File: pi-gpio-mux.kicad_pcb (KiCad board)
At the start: 2 copper layers, 65 x 56 mm, 35 parts, among them J1 Raspberry_Pi_2_3, J2 Raw, J3 Buffered, J4 Register-1, J5 Register-2, J6 Clk1, J7 Clk2, U1 74AHCT245, U10 74AHCT574, U11 74AHCT574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

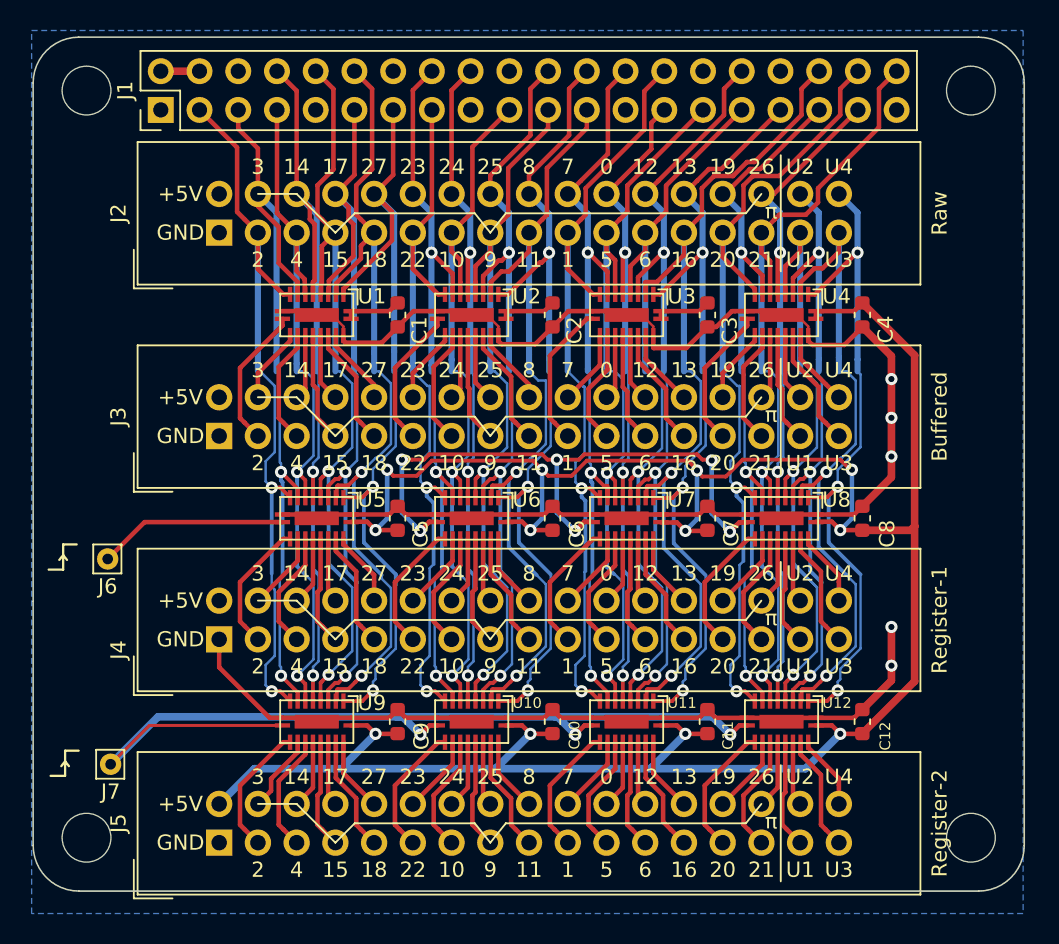
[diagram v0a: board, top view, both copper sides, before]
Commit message: Solve routing of VCC for buffers.
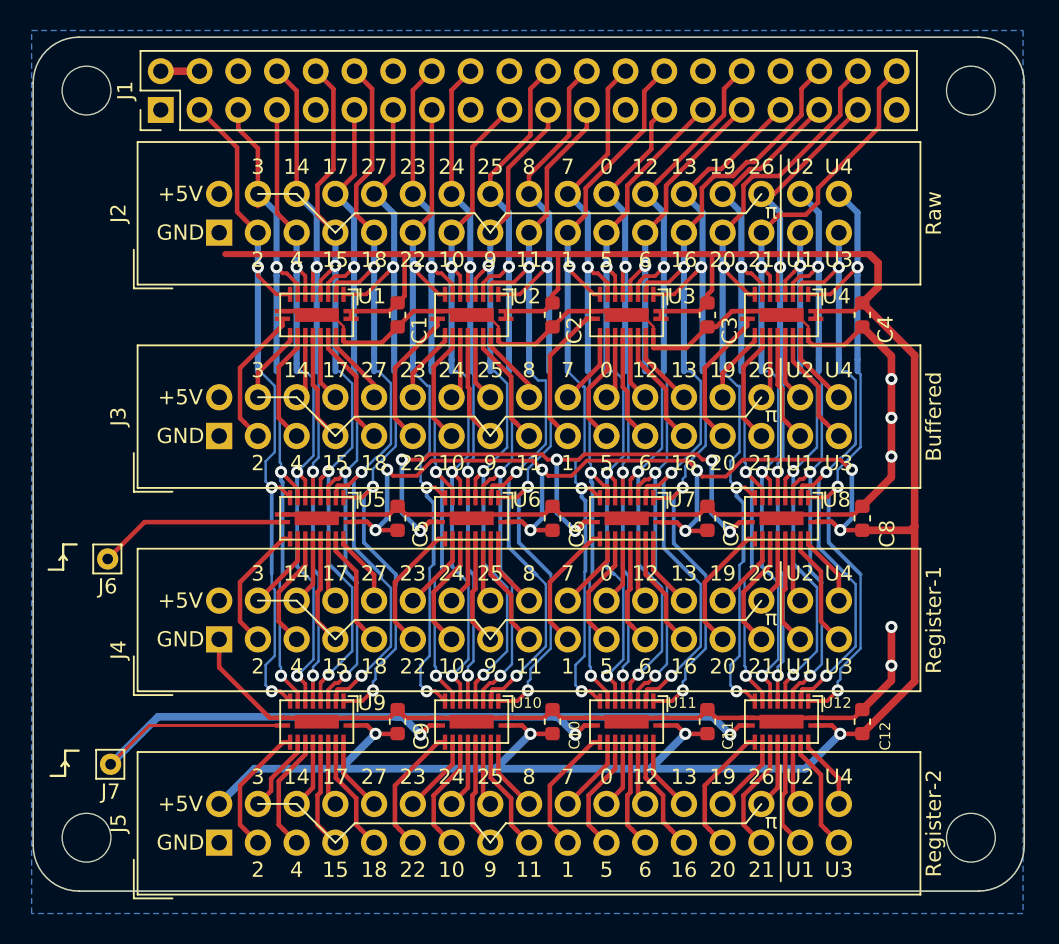
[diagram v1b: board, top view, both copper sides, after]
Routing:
- net VCC: track 180.9 -> 237.2 mm
- net Pin8-GPIO14: track 51.7 -> 46.4 mm, vias 2 -> 3
- net Pin11-GPIO17: track 51.5 -> 46.6 mm, vias 2 -> 3
- net Pin13-GPIO27: track 54.4 -> 50.0 mm, vias 2 -> 3
- net Pin5-GPIO3: track 50.3 -> 45.9 mm, vias 2 -> 3
- net Pin15-GPIO22: track 48.4 -> 46.1 mm, vias 2 -> 3
- net Pin28-GPIO1: track 52.9 -> 50.6 mm, vias 2 -> 3
- net Pin7-GPIO4: track 48.2 -> 45.9 mm, vias 2 -> 3
- net Pin19-GPIO10: track 49.0 -> 46.7 mm, vias 2 -> 3
- net Pin40-GPIO21: track 54.7 -> 52.4 mm, vias 2 -> 3
- net Pin29-GPIO5: track 50.1 -> 47.8 mm, vias 2 -> 3
- net Pin21-GPIO9: track 50.6 -> 48.4 mm, vias 2 -> 3
- net Pin10-GPIO15: track 51.9 -> 49.7 mm, vias 2 -> 3
- net Pin31-GPIO6: track 51.9 -> 49.7 mm, vias 2 -> 3
- net User1: track 41.1 -> 39.0 mm, vias 2 -> 3
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
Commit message: Route VCC and GND. No unrouted left.
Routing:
- net VCC: track 237.2 -> 350.9 mm, vias 12 -> 13
- net /CLK1: track 53.0 -> 70.9 mm
- net /CLK2: track 62.7 -> 53.3 mm, vias 3 -> 4
- net GND: track 155.2 -> 162.6 mm, vias 5 -> 7
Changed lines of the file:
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@@
     (thickness 1.6)
     (drawings 21)
-    (tracks 1649)
+    (tracks 1692)
     (zones 0)
     (modules 35)
@@
   )
   (setup
-    (last_trace_width 0.3)
+    (last_trace_width 0.25)
     (user_trace_width 0.16)
     (user_trace_width 0.2)
@@
   (via (at 256.2864 135.2172) (size 0.8) (drill 0.4) (layers F.Cu B.Cu) (net 1))
   (via (at 256.2864 132.6772) (size 0.8) (drill 0.4) (layers F.Cu B.Cu) (net 1))
+  (via (at 213.3984 124.5492) (size 0.8) (drill 0.4) (layers F.Cu B.Cu) (net 1))
+  (segment (start 216.35 125.3025) (end 214.1517 125.3025) (width 0.25) (layer F.Cu) (net 1))
+  (segment (start 214.1517 125.3025) (end 213.3984 124.5492) (width 0.25) (layer F.Cu) (net 1))
+  (via (at 212.23 111.9508) (size 0.8) (drill 0.4) (layers F.Cu B.Cu) (net 1))
+  (segment (start 216.35 111.9675) (end 212.2467 111.9675) (width 0.25) (layer F.Cu) (net 1))
+  (segment (start 212.2467 111.9675) (end 212.23 111.9508) (width 0.25) (layer F.Cu) (net 1))
   (segment (start 243.884799 122.815599) (end 243.4848 122.4156) (width 0.25) (layer F.Cu) (net 2))
   (segment (start 245.423799 122.815599) (end 243.884799 122.815599) (width 0.25) (layer F.Cu) (net 2))
@@
   (segment (start 214.5114 141.9736) (end 220.4724 141.9736) (width 0.5) (layer B.Cu) (net 2))
   (segment (start 220.4724 141.9736) (end 230.1244 141.9736) (width 0.5) (layer B.Cu) (net 2))
-  (segment (start 210.91 96.23) (end 208.37 96.23) (width 0.5) (layer F.Cu) (net 2))
+  (segment (start 210.91 96.23) (end 208.37 96.23) (width 1) (layer F.Cu) (net 2))
   (segment (start 254.38 111.43) (end 257.8104 114.8604) (width 0.5) (layer F.Cu) (net 2))
   (segment (start 257.8104 136.2446) (end 254.38 139.675) (width 0.5) (layer F.Cu) (net 2))
@@
   (segment (start 255.41 108.8012) (end 254.902 108.2932) (width 0.5) (layer F.Cu) (net 2))
   (segment (start 254.902 108.2932) (end 254.836276 108.227476) (width 0.4) (layer F.Cu) (net 2))
-  (segment (start 224.254674 108.227474) (end 212.600526 108.227474) (width 0.4) (layer F.Cu) (net 2))
   (segment (start 254.836272 108.227472) (end 254.902 108.2932) (width 0.4) (layer F.Cu) (net 2))
   (segment (start 234.4296 110.5229) (end 234.4296 108.344) (width 0.3) (layer F.Cu) (net 2))
@@
   (segment (start 224.361612 108.309896) (end 224.361612 110.968388) (width 0.3) (layer F.Cu) (net 2))
   (segment (start 224.3204 108.268684) (end 224.361612 108.309896) (width 0.3) (layer F.Cu) (net 2))
+  (segment (start 223.2156 122.3648) (end 222.606 121.7552) (width 0.2) (layer F.Cu) (net 2))
+  (segment (start 222.606 121.7552) (end 214.8208 121.7552) (width 0.2) (layer F.Cu) (net 2))
+  (segment (start 207.520001 97.079999) (end 207.171999 97.079999) (width 1) (layer F.Cu) (net 2))
+  (segment (start 207.171999 97.079999) (end 206.5912 97.660798) (width 1) (layer F.Cu) (net 2))
+  (segment (start 201.1556 133.2406) (end 212.2 144.285) (width 1) (layer F.Cu) (net 2))
+  (segment (start 206.5912 97.660798) (end 206.5912 99.6572) (width 1) (layer F.Cu) (net 2))
+  (segment (start 208.37 96.23) (end 207.520001 97.079999) (width 1) (layer F.Cu) (net 2))
+  (segment (start 201.6128 130.95) (end 201.1556 130.4928) (width 1) (layer F.Cu) (net 2))
+  (segment (start 212.2 130.95) (end 201.6128 130.95) (width 1) (layer F.Cu) (net 2))
+  (segment (start 201.1556 105.0928) (end 201.1556 130.4928) (width 1) (layer F.Cu) (net 2))
+  (segment (start 201.1556 130.4928) (end 201.1556 133.2406) (width 1) (layer F.Cu) (net 2))
+  (segment (start 212.2 117.615) (end 210.0964 115.5114) (width 1) (layer F.Cu) (net 2))
+  (segment (start 210.978686 104.28) (end 212.2 104.28) (width 1) (layer F.Cu) (net 2))
+  (segment (start 210.0964 105.162286) (end 210.978686 104.28) (width 1) (layer F.Cu) (net 2))
+  (segment (start 210.1472 104.28) (end 206.0578 100.1906) (width 1) (layer F.Cu) (net 2))
+  (segment (start 212.2 104.28) (end 210.1472 104.28) (width 1) (layer F.Cu) (net 2))
+  (segment (start 206.5912 99.6572) (end 206.0578 100.1906) (width 1) (layer F.Cu) (net 2))
+  (segment (start 206.0578 100.1906) (end 201.1556 105.0928) (width 1) (layer F.Cu) (net 2))
+  (segment (start 210.538674 108.227474) (end 210.0964 107.7852) (width 0.4) (layer F.Cu) (net 2))
+  (segment (start 224.254674 108.227474) (end 210.538674 108.227474) (width 0.4) (layer F.Cu) (net 2))
+  (segment (start 210.0964 115.5114) (end 210.0964 107.7852) (width 1) (layer F.Cu) (net 2))
+  (segment (start 210.0964 107.7852) (end 210.0964 105.162286) (width 1) (layer F.Cu) (net 2))
+  (segment (start 214.8208 121.7552) (end 214.516 121.7552) (width 0.3) (layer F.Cu) (net 2))
+  (segment (start 214.516 121.7552) (end 213.8556 121.7552) (width 0.3) (layer F.Cu) (net 2))
+  (via (at 211.214 124.6) (size 0.8) (drill 0.4) (layers F.Cu B.Cu) (net 2))
+  (segment (start 213.8556 121.7552) (end 211.214 124.3968) (width 0.3) (layer F.Cu) (net 2))
+  (segment (start 211.214 124.3968) (end 211.214 124.6) (width 0.3) (layer F.Cu) (net 2))
+  (segment (start 211.214 129.964) (end 212.2 130.95) (width 0.3) (layer B.Cu) (net 2))
+  (segment (start 211.214 124.6) (end 211.214 129.964) (width 0.3) (layer B.Cu) (net 2))
   (segment (start 247.79264 128.70464) (end 247.79264 122.93376) (width 0.25) (layer B.Cu) (net 3))
   (segment (start 248.26 129.172) (end 247.79264 128.70464) (width 0.25) (layer B.Cu) (net 3))
@@
   (segment (start 234.3408 125.185147) (end 235.135391 125.979738) (width 0.3) (layer B.Cu) (net 132))
   (segment (start 236.67 125.7771) (end 236.138027 125.7771) (width 0.3) (layer F.Cu) (net 132))
-  (segment (start 207.3065 125.8025) (end 204.8895 128.2195) (width 0.3) (layer F.Cu) (net 132))
-  (segment (start 216.35 125.8025) (end 207.3065 125.8025) (width 0.3) (layer F.Cu) (net 132))
+  (segment (start 224.1808 121.7044) (end 223.755001 121.278601) (width 0.2) (layer F.Cu) (net 132))
+  (segment (start 207.3065 125.8025) (end 207.1945 125.9145) (width 0.3) (layer F.Cu) (net 132))
+  (segment (start 207.1945 125.9145) (end 204.8895 128.2195) (width 0.3) (layer F.Cu) (net 132))
+  (segment (start 216.35 125.8025) (end 212.4673 125.8025) (width 0.3) (layer F.Cu) (net 132))
+  (segment (start 223.755001 121.278601) (end 213.887001 121.278601) (width 0.2) (layer F.Cu) (net 132))
+  (segment (start 213.862001 121.303601) (end 212.800599 121.303601) (width 0.25) (layer F.Cu) (net 132))
+  (segment (start 213.887001 121.278601) (end 213.862001 121.303601) (width 0.25) (layer F.Cu) (net 132))
+  (segment (start 212.4673 125.8025) (end 208.3017 125.8025) (width 0.3) (layer F.Cu) (net 132))
+  (segment (start 212.800599 121.303601) (end 208.3017 125.8025) (width 0.25) (layer F.Cu) (net 132))
+  (segment (start 208.3017 125.8025) (end 207.3065 125.8025) (width 0.3) (layer F.Cu) (net 132))
   (segment (start 246.83 139.1375) (end 246.3209 139.1375) (width 0.3) (layer F.Cu) (net 133))
   (segment (start 246.3209 139.1375) (end 245.72 139.7384) (width 0.3) (layer F.Cu) (net 133))
@@
   (segment (start 208.1915 138.57) (end 223.8252 138.57) (width 0.5) (layer B.Cu) (net 133))
   (segment (start 223.8252 138.57) (end 234.2392 138.57) (width 0.5) (layer B.Cu) (net 133))
-  (segment (start 207.624 139.1375) (end 205.08 141.6815) (width 0.2) (layer F.Cu) (net 133))
-  (segment (start 216.35 139.1375) (end 207.624 139.1375) (width 0.2) (layer F.Cu) (net 133))
+  (via (at 213.6524 138.6208) (size 0.8) (drill 0.4) (layers F.Cu B.Cu) (net 133))
+  (segment (start 216.35 139.1375) (end 214.1691 139.1375) (width 0.3) (layer F.Cu) (net 133))
+  (segment (start 214.1691 139.1375) (end 213.6524 138.6208) (width 0.3) (layer F.Cu) (net 133))
   (segment (start 254.263612 129.232012) (end 252.1716 127.14) (width 0.25) (layer B.Cu) (net 134))
   (segment (start 252.1716 127.14) (end 252.1716 124.075062) (width 0.25) (layer B.Cu) (net 134))

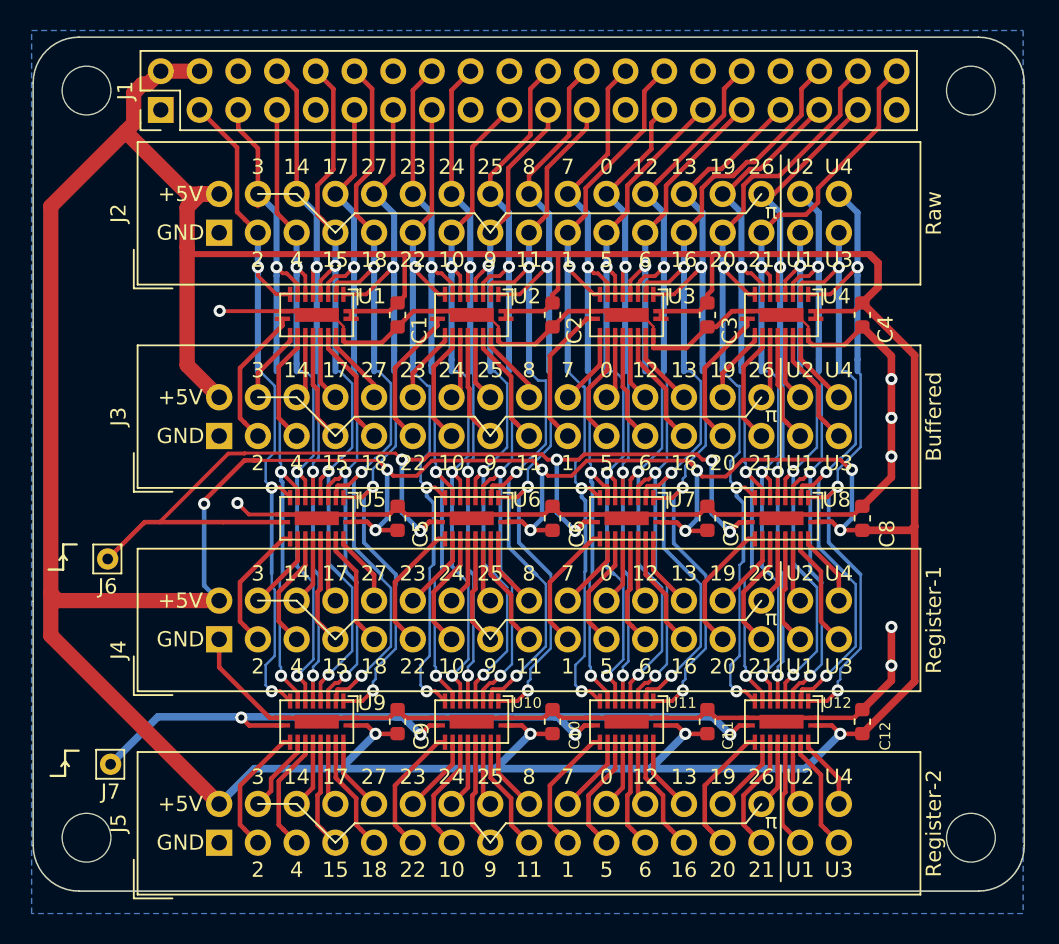
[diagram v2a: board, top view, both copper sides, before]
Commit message: Add inverters.
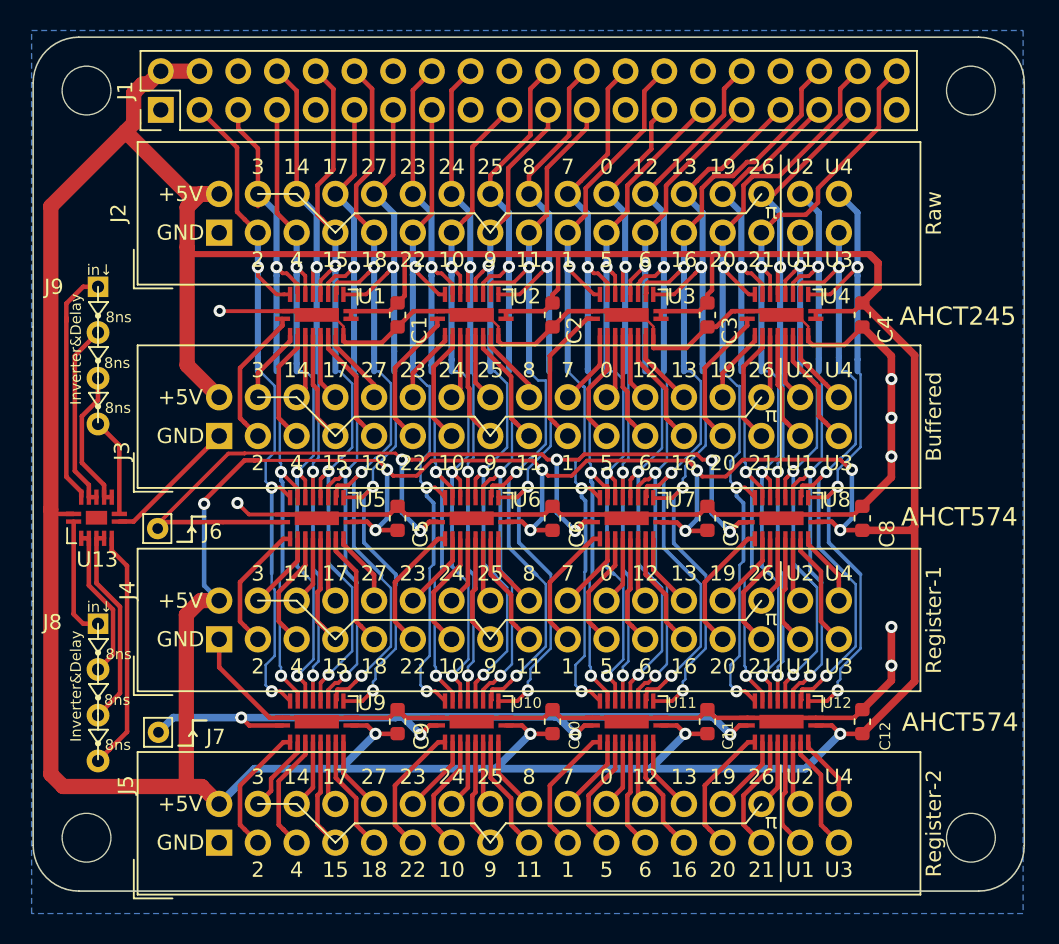
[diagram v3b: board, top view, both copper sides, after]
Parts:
- added J8: Conn_01x04, pi-gpio-mux:triple-inverter, F.Cu at (204.3, 132.5)
- added J9: Conn_01x04, pi-gpio-mux:triple-inverter, F.Cu at (204.3, 110.4)
- added U13: 74HCT04, pi-gpio-mux:SOT762-1-DHVQFN14, F.Cu at (204.2, 125.5)
- moved J6 3.84 mm to (208.2, 126.2)
- moved J7 3.77 mm to (208.2, 139.6)
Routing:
- net Net-(J9-Pad1): track 0.00 -> 15.8 mm
- net Net-(J8-Pad4): track 0.00 -> 15.8 mm
- net Net-(J8-Pad3): track 0.00 -> 13.3 mm
- net Net-(J9-Pad2): track 0.00 -> 12.3 mm
- net Net-(J8-Pad2): track 0.00 -> 10.2 mm
- net VCC: track 350.9 -> 360.4 mm
- net Net-(J9-Pad3): track 0.00 -> 9.34 mm
- net GND: track 162.6 -> 171.4 mm
- net Net-(J8-Pad1): track 0.00 -> 7.94 mm
- net Net-(J9-Pad4): track 0.00 -> 6.48 mm
- net /CLK1: track 70.9 -> 66.8 mm
- net /CLK2: track 53.3 -> 49.3 mm
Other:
- board text added: "AHCT245"
- board text added: "AHCT574"

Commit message: More copper clearance around screw holes; add VCC pour on top layer.
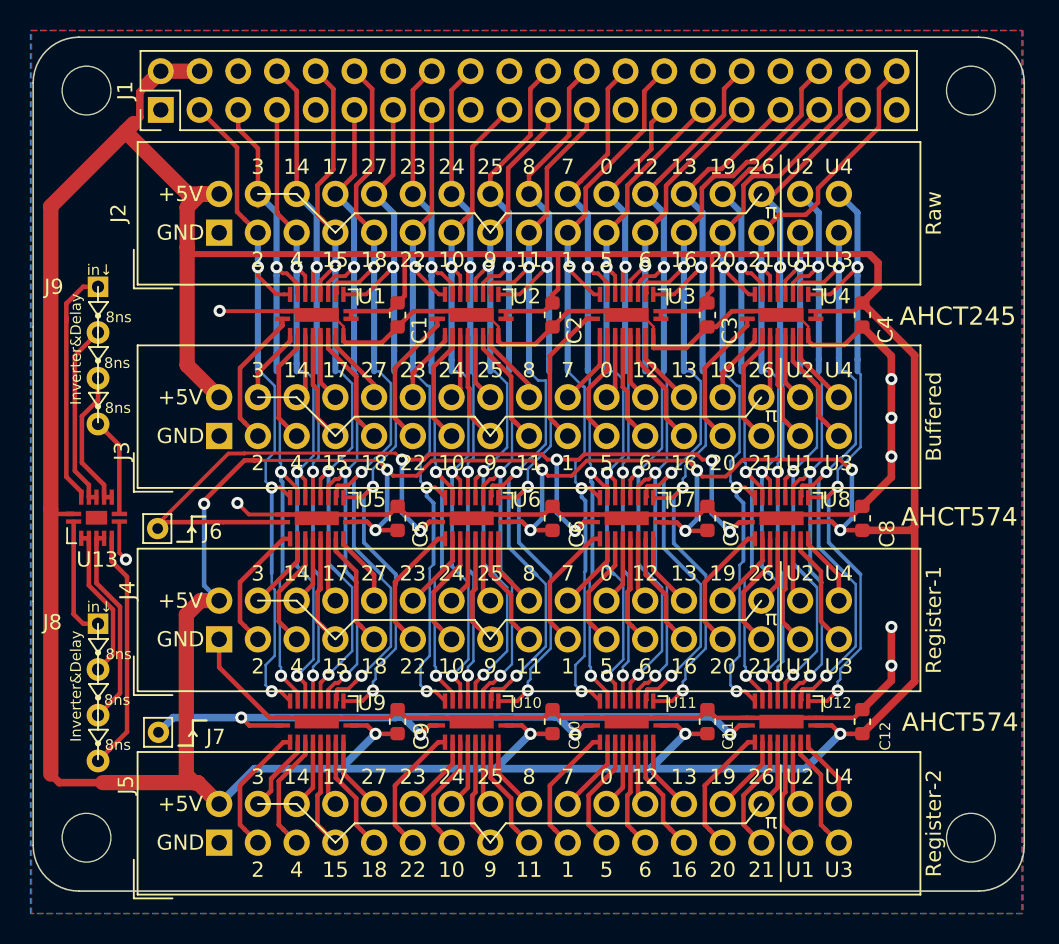
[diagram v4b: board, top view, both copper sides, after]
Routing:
- net GND: track 171.4 -> 165.2 mm, vias 7 -> 8
- added copper zone on F.Cu, net VCC

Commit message: Improve 1 marker packages; add %%gitversion%% and Makefile to create fab.
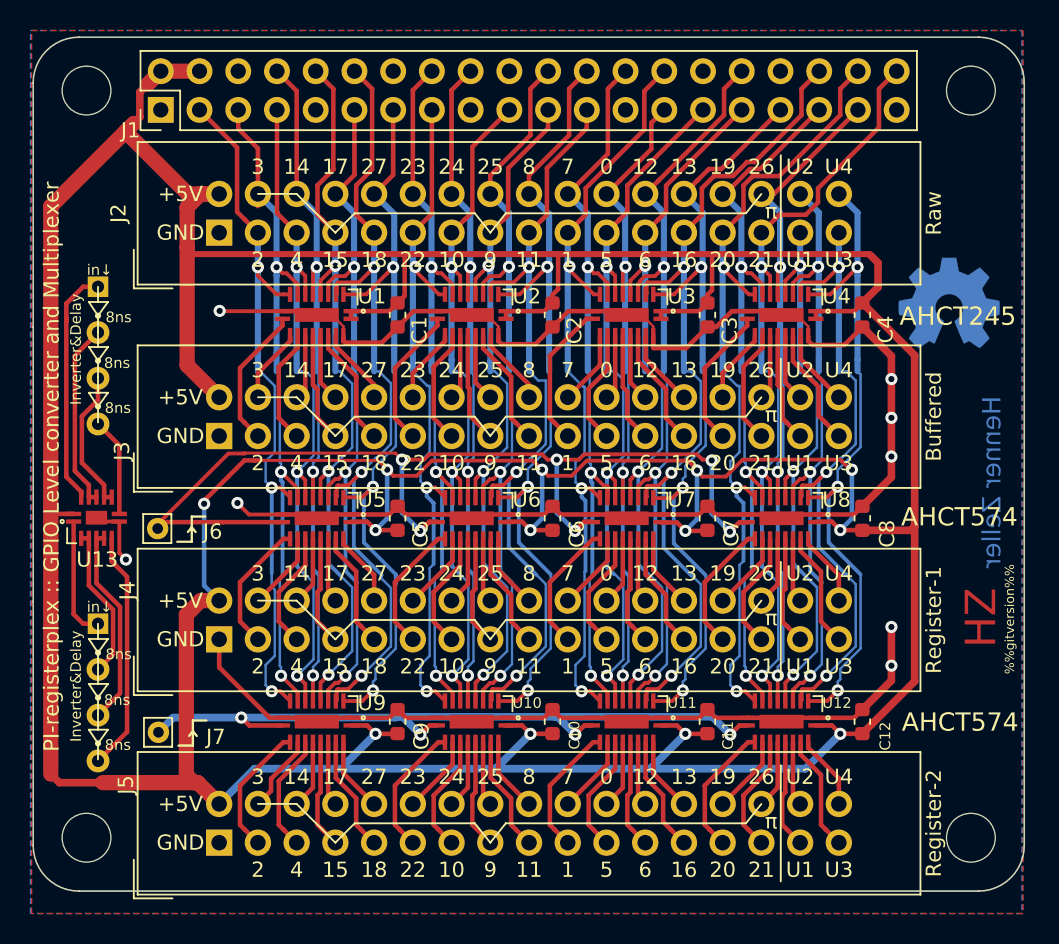
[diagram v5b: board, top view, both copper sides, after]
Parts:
- added REF**: OSHW-Symbol_6.7x6mm_Copper, Symbol:OSHW-Symbol_6.7x6mm_Copper, B.Cu at (260.1, 111.4)
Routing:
- net GND: track 165.2 -> 166.9 mm
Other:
- rule solder_mask_min_width: 0.25 -> 0.2
- board text added: "%%gitversion%%"
- board text added: "%%gitversion%% github.com/hzeller/pi-registerplex"
- board text added: "HZ"
- board text added: "Henner Zeller"
- board text added: "PI-registerplex :: GPIO Level converter and Multiplexer"
